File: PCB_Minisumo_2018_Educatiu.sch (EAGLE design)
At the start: 91 parts, among them Q1 BC817, Q2 BC817, Q3 BC817

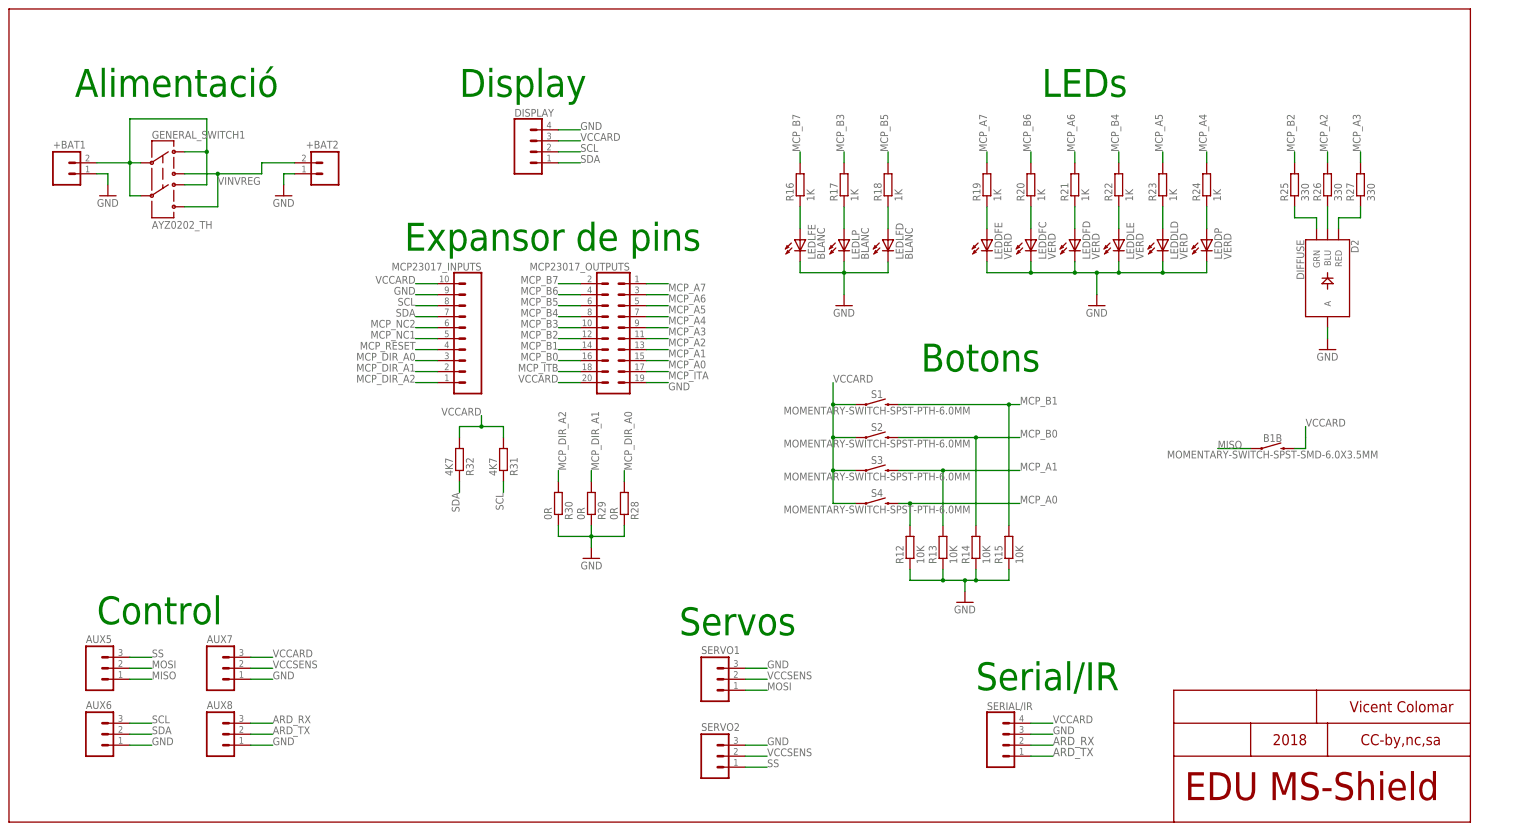
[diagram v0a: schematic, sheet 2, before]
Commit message: Add files via upload
Corregits petits defectes en la placa.
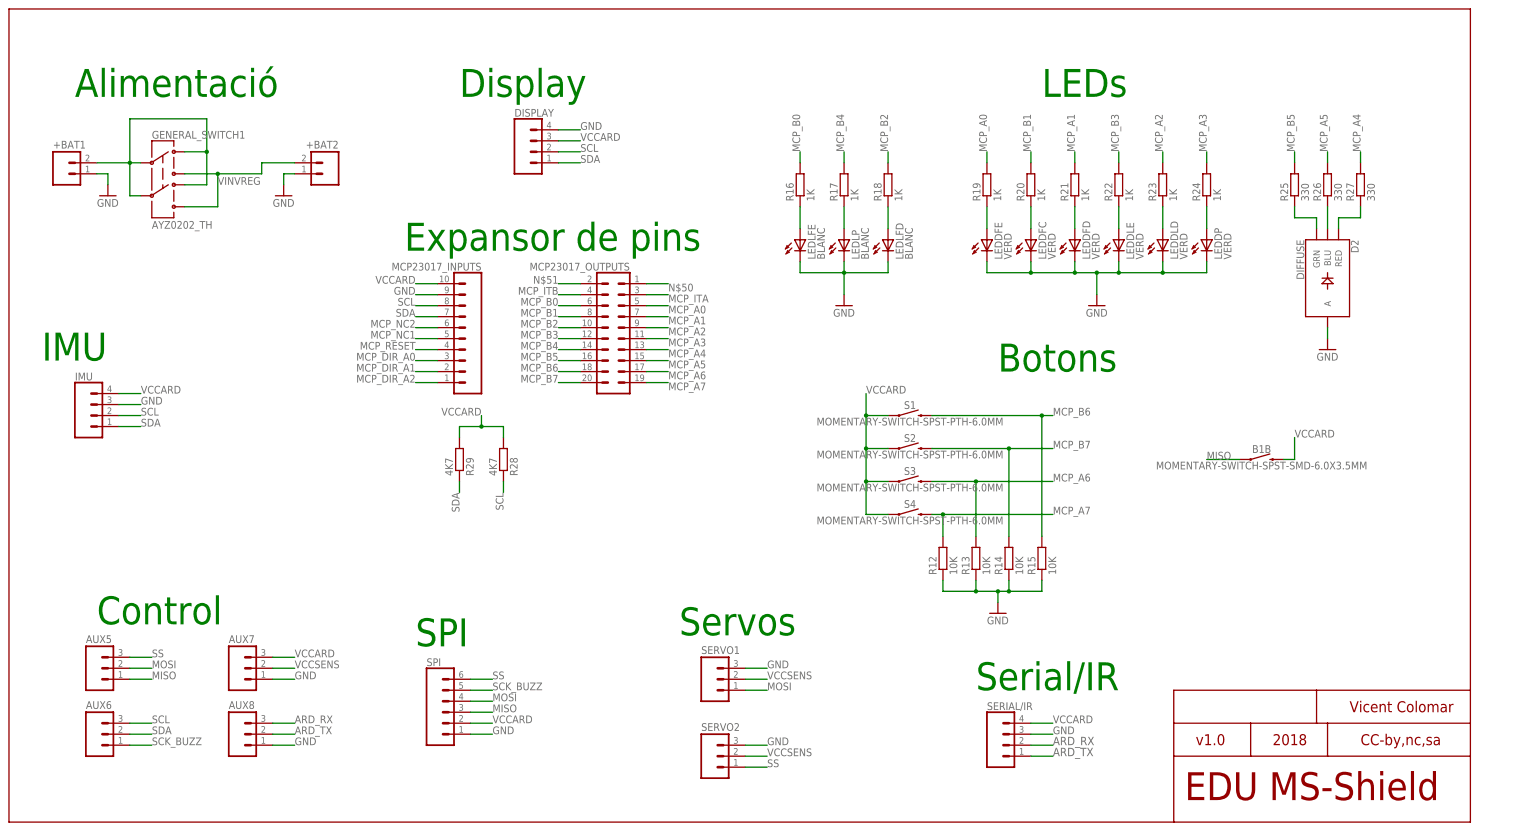
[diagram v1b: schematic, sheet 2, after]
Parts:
- removed R30: 0R, rcl:R-EU_M1206
- removed R31, R32: 4K7, rcl:R-EU_M1206
- added IMU: (no value), SparkFun-Connectors:CONN_04
- added J1: (no value), SparkFun-Connectors:CONN_02
- added SPI: (no value), SparkFun-Connectors:CONN_06SILK_FEMALE_PTH
- R28, R29: value 0R -> 4K7
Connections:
- removed net BUZZ: R3.1, U$1.D13
- new net N$1: J1.2, R3.1
- new net N$50: MCP23017_OUTPUTS.1
- new net N$51: MCP23017_OUTPUTS.2
- new net SCK_BUZZ: AUX2.1, AUX6.1, J1.1, SPI.5, U$1.D13
- net GND: now also IMU.3, SPI.1; no longer AUX2.1, AUX6.1, MCP23017_OUTPUTS.19, R28.1, R29.1, R30.1
- net MCP_A0: now also MCP23017_OUTPUTS.5, R19.2; no longer MCP23017_OUTPUTS.15, R12.2, S4.2
- net MCP_A1: now also MCP23017_OUTPUTS.7, R21.2; no longer MCP23017_OUTPUTS.13, R13.2, S3.2
- net MCP_A2: now also MCP23017_OUTPUTS.9, R23.2; no longer MCP23017_OUTPUTS.11, R26.2
- net MCP_A3: now also MCP23017_OUTPUTS.11, R24.2; no longer MCP23017_OUTPUTS.9, R27.2
- net MCP_A4: now also MCP23017_OUTPUTS.13, R27.2; no longer MCP23017_OUTPUTS.7, R24.2
- net MCP_A5: now also MCP23017_OUTPUTS.15, R26.2; no longer MCP23017_OUTPUTS.5, R23.2
- net MCP_A6: now also MCP23017_OUTPUTS.17, R13.2, S3.2; no longer MCP23017_OUTPUTS.3, R21.2
- net MCP_A7: now also MCP23017_OUTPUTS.19, R12.2, S4.2; no longer MCP23017_OUTPUTS.1, R19.2
- net MCP_B0: now also MCP23017_OUTPUTS.6, R16.2; no longer MCP23017_OUTPUTS.16, R14.2, S2.2
- net MCP_B1: now also MCP23017_OUTPUTS.8, R20.2; no longer MCP23017_OUTPUTS.14, R15.2, S1.2
- net MCP_B2: now also MCP23017_OUTPUTS.10, R18.2; no longer MCP23017_OUTPUTS.12, R25.2
- net MCP_B3: now also MCP23017_OUTPUTS.12, R22.2; no longer MCP23017_OUTPUTS.10, R17.2
- net MCP_B4: now also MCP23017_OUTPUTS.14, R17.2; no longer MCP23017_OUTPUTS.8, R22.2
- net MCP_B5: now also MCP23017_OUTPUTS.16, R25.2; no longer MCP23017_OUTPUTS.6, R18.2
- net MCP_B6: now also MCP23017_OUTPUTS.18, R15.2, S1.2; no longer MCP23017_OUTPUTS.4, R20.2
- net MCP_B7: now also MCP23017_OUTPUTS.20, R14.2, S2.2; no longer MCP23017_OUTPUTS.2, R16.2
- net MCP_DIR_A0: no longer R28.2
- net MCP_DIR_A1: no longer R29.2
- net MCP_DIR_A2: no longer R30.2
- net MCP_ITA: now also MCP23017_OUTPUTS.3; no longer MCP23017_OUTPUTS.17
- net MCP_ITB: now also MCP23017_OUTPUTS.4; no longer MCP23017_OUTPUTS.18
- net MISO: now also SPI.3
- net MOSI: now also SPI.4
- net SCL: now also IMU.2, R28.1; no longer R31.1
- net SDA: now also IMU.1, R29.1; no longer R32.1
- net SS: now also SPI.6
- net VCCARD: now also IMU.4, R28.2, R29.2, SPI.2; no longer MCP23017_OUTPUTS.20, R31.2, R32.2
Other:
- note added: "IMU"
- note added: "SPI"
- note added: "v1.0"
- moved on the sheet: AUX7, AUX8, B1, B1B, R1, R12, R13, R14, R15, R28, R29, S1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
